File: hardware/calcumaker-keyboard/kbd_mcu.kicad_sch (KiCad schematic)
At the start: 8 parts, among them J2 SWD TC2030-NL, U1 STM32G031K8U6

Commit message: hardware: MCU -> STM32U575RGT6 (LQFP-64) + 4MB QSPI flash; monospace wiring notes
MCU package + external flash
- Swap U1 STM32U575ZGT6 (LQFP-144) -> STM32U575RGT6 (LQFP-64, LCSC C5270980).
  The firmware links at ~323 KB so 1 MB flash is ample (~3x headroom), and with
  the key matrix scanned off-board the LQFP-64 has enough GPIO — smaller/cheaper.
- Correct the flash size everywhere: the STM32 `G` code = 1 MB (not 2 MB; the
  `I` parts are 2 MB). memory.x FLASH 2048K -> 1024K; .cargo runner -> RGTx.
- Add U7 W25Q32JVSSIQ, a 4 MB (32 Mbit) quad-SPI NOR (LCSC C179173, SOIC-8) on
  OCTOSPI1 as a new QSPIFlash sheet (+ R9 CS# pull-up + C26 decoupling) for
  memory-mapped (XIP) constants + state/program storage.
- mcu board 52 -> 55 components / 7 sheets. Docs (DESIGN.md, PARTS.md, READMEs,
  CLAUDE/AGENTS) updated; availability ladder now lists RGT6/VGT6/ZGT6.

Monospace, multi-line schematic wiring notes
- kschgen text_note() now renders notes in a monospace font (Courier New) so
  tables/columns line up; add note_block() + pin_table() helpers.
- Reformat all 14 per-sheet notes into titled, multi-line, aligned blocks —
  connector pinouts as PIN/SIGNAL tables, power/MCU sheets as wiring blocks.

The regenerated schematics carry both changes, so this is one commit. All three
boards regenerate + pass the structure check (mcu 55 / keyboard 119 / display
60, no duplicate refs).

Co-Authored-By: Claude Opus 4.8 (1M context) <noreply@anthropic.com>
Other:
- note added: "SCANNER MCU - U1 STM32G031K8U6 (LCSC C432207, UFQFPN-32) PLACED, not wired. POWER VDD -> +3V3 C1/C2 100nF + C4 4.7uF bulk VDDA -> C3 100nF VSS/EP -> GND RESET / BOOT NRST -> C5 100nF (also -> KB_NRST on J1: U575 can reset it) BOOT0 -> R6 10k to GND (also -> KB_BOOT0 on J1: ROM UART/DFU reflash) CLOCK internal HSI, no crystal. MATRIX 5 ROW (out) + 10 COL (in, int. pull-ups) -> Keypad sheet; hold R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"
- note removed: "Calcumaker 16 keyboard — Scanner MCU U1 STM32G031K8U6 (LCSC C432207, UFQFPN-32). PLACED, not wired. POWER: VDD -> +3V3 (C1/C2 100nF + C4 4.7uF bulk); VDDA -> C3 100nF; VSS/EP -> GND. RESET: NRST + C5 100nF (also -> KB_NRST on J1 so the MCU can reset it). BOOT0 -> R6 10k to GND (also -> KB_BOOT0 on J1 for ROM UART/DFU reflash). CLOCK: internal HSI, no crystal. MATRIX: 5 ROW (out) + 10 COL (in, int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"
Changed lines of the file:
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@@
 		(instances
 			(project "calcumaker-keyboard"
-				(path "/ca1c0000-0000-4000-8000-00000000eb01/6aa00c6d-c4c7-4ac8-98e2-2764bb39a4cb"
+				(path "/ca1c0000-0000-4000-8000-00000000eb01/4dd7cdeb-aa77-4ab0-b654-f9a7d07f70a8"
 					(reference "U1")
 					(unit 1)
@@
 		(instances
 			(project "calcumaker-keyboard"
-				(path "/ca1c0000-0000-4000-8000-00000000eb01/6aa00c6d-c4c7-4ac8-98e2-2764bb39a4cb"
+				(path "/ca1c0000-0000-4000-8000-00000000eb01/4dd7cdeb-aa77-4ab0-b654-f9a7d07f70a8"
 					(reference "C1")
 					(unit 1)
@@
 		(instances
 			(project "calcumaker-keyboard"
-				(path "/ca1c0000-0000-4000-8000-00000000eb01/6aa00c6d-c4c7-4ac8-98e2-2764bb39a4cb"
+				(path "/ca1c0000-0000-4000-8000-00000000eb01/4dd7cdeb-aa77-4ab0-b654-f9a7d07f70a8"
 					(reference "C2")
 					(unit 1)
@@
 		(instances
 			(project "calcumaker-keyboard"
-				(path "/ca1c0000-0000-4000-8000-00000000eb01/6aa00c6d-c4c7-4ac8-98e2-2764bb39a4cb"
+				(path "/ca1c0000-0000-4000-8000-00000000eb01/4dd7cdeb-aa77-4ab0-b654-f9a7d07f70a8"
 					(reference "C3")
 					(unit 1)
@@
 		(instances
 			(project "calcumaker-keyboard"
-				(path "/ca1c0000-0000-4000-8000-00000000eb01/6aa00c6d-c4c7-4ac8-98e2-2764bb39a4cb"
+				(path "/ca1c0000-0000-4000-8000-00000000eb01/4dd7cdeb-aa77-4ab0-b654-f9a7d07f70a8"
 					(reference "C4")
 					(unit 1)
@@
 		(instances
 			(project "calcumaker-keyboard"
-				(path "/ca1c0000-0000-4000-8000-00000000eb01/6aa00c6d-c4c7-4ac8-98e2-2764bb39a4cb"
+				(path "/ca1c0000-0000-4000-8000-00000000eb01/4dd7cdeb-aa77-4ab0-b654-f9a7d07f70a8"
 					(reference "C5")
 					(unit 1)
@@
 		(instances
 			(project "calcumaker-keyboard"
-				(path "/ca1c0000-0000-4000-8000-00000000eb01/6aa00c6d-c4c7-4ac8-98e2-2764bb39a4cb"
+				(path "/ca1c0000-0000-4000-8000-00000000eb01/4dd7cdeb-aa77-4ab0-b654-f9a7d07f70a8"
 					(reference "R6")
 					(unit 1)
@@
 		(instances
 			(project "calcumaker-keyboard"
-				(path "/ca1c0000-0000-4000-8000-00000000eb01/6aa00c6d-c4c7-4ac8-98e2-2764bb39a4cb"
+				(path "/ca1c0000-0000-4000-8000-00000000eb01/4dd7cdeb-aa77-4ab0-b654-f9a7d07f70a8"
 					(reference "J2")
 					(unit 1)
@@
 		)
 	)
-	(text "Calcumaker 16 keyboard — Scanner MCU U1 STM32G031K8U6 (LCSC C432207, UFQFPN-32). PLACED, not wired. POWER: VDD -> +3V3 (C1/C2 100nF + C4 4.7uF bulk); VDDA -> C3 100nF; VSS/EP -> GND. RESET: NRST + C5 100nF (also -> KB_NRST on J1 so the MCU can reset it). BOOT0 -> R6 10k to GND (also -> KB_BOOT0 on J1 for ROM UART/DFU reflash). CLOCK: internal HSI, no crystal. MATRIX: 5 ROW (out) + 10 COL (in, internal pull-ups) -> Keypad sheet; hold ROWs low + COL EXTI for wake-from-Stop. ANNUNCIATORS: 5 GPIO -> the LED resistors (Annunciators sheet). LINK to the U575 (via J1 mezzanine): I2C1 SDA/SCL (reports keys, receives annunciator state) + USART TX/RX (alt/expansion + bootloader) + KB_IRQ out (wakes the U575). PROGRAMMING: J2 SWD Tag-Connect (bare pads) or the UART/DFU bootloader over J1. See DESIGN.md Low-power & wake."
+	(text "SCANNER MCU  -  U1  STM32G031K8U6  (LCSC C432207, UFQFPN-32)\nPLACED, not wired.\n\nPOWER\n  VDD  -> +3V3   C1/C2 100nF + C4 4.7uF bulk\n  VDDA -> C3 100nF          VSS/EP -> GND\nRESET / BOOT\n  NRST  -> C5 100nF  (also -> KB_NRST on J1: U575 can reset it)\n  BOOT0 -> R6 10k to GND (also -> KB_BOOT0 on J1: ROM UART/DFU reflash)\nCLOCK   internal HSI, no crystal.\n\nMATRIX  5 ROW (out) + 10 COL (in, int. pull-ups) -> Keypad sheet;\n        hold ROWs low + COL EXTI for wake-from-Stop.\nANNUN   5 GPIO -> the LED resistors (Annunciators sheet).\nLINK (via J1 mezzanine to the U575)\n  I2C1  SDA/SCL  reports keys, receives annunciator state\n  USART TX/RX    alt/expansion + bootloader\n  KB_IRQ (out)   wakes the U575\nPROG    J2 SWD Tag-Connect (bare pads) or UART/DFU over J1.\nSee DESIGN.md Low-power & wake."
 		(exclude_from_sim no)
 		(at 15.00 150.00 0)
-		(effects (font (size 1.5 1.5)) (justify left top))
+		(effects (font (face "Courier New") (size 1.27 1.27)) (justify left top))
 	)
 	(sheet_instances

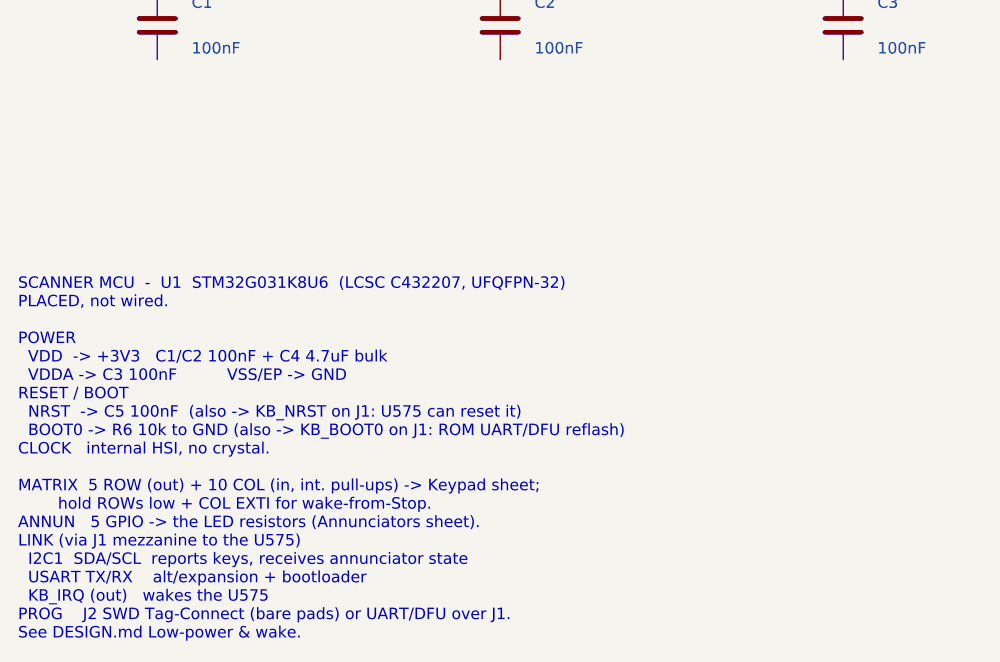
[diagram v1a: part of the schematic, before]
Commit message: hardware: per-key RGB hint lighting on the keyboard board (50x SK6805 on gated VSYS) (#4)
Add addressable RGB accent lighting that hints key positions / presses -- one
SK6805-EC15 (1.5x1.5mm, the smallest serial RGB with a KiCad footprint + real
LCSC stock, C2890035) beside each of the 50 keys, single-wire daisy chain off
one STM32G0 pin.

Power: the LEDs are ~5V parts and the keyboard rail is only 3.3V, so they run
off VSYS (the MCU board's load-shared battery/USB rail, ~3.7-4.7V) brought up a
WIDENED 12-pin mezzanine (10 -> 12: +VSYS +GND). A high-side P-FET load switch
(Q1 AO3401A + Q2 2N7002) gates the whole LED rail off in sleep (G0 LED_EN) to
protect battery life, and a 74LVC1G125 (powered from the gated rail) level-shifts
the 3.3V data up to the LED VIH.

- calcumaker-keyboard: new KeyLighting sheet (50x SK6805 D56-D105 + U2 shifter +
  Q1/Q2 load switch + R7-R10 / C6-C7); J1 mezzanine -> 12-pin DF40C-12DP
  (C6224952). 119 -> 178 components.
- calcumaker-mcu: J5 mezzanine -> 12-pin DF40B-12DS (C3641147); route VSYS.
- DF40 stack: the receptacle SUFFIX sets the mated height (none = 1.5mm,
  (2.0) = 2.0mm, H-series = 2.5-4.0mm), NOT the B/C letter; the DF40C plug is the
  common header -- so DF40C-12DP x DF40B-12DS is a valid 1.5mm stack, same as the
  original 10-pin (DF40C-12DS just isn't LCSC-stocked).
- DESIGN.md / PARTS.md / memory: RGB subsystem, 12-pin pinout, BOM rows, the
  sleep-gate + current-cap notes (firmware must cap total brightness; 50x
  full-white ~0.75A would exceed the DF40 / VSYS budget).

All three boards regenerate + pass the structure check (mcu 55 / keyboard 178 /
display 60, no duplicate refs).

Co-authored-by: Claude Opus 4.8 (1M context) <noreply@anthropic.com>
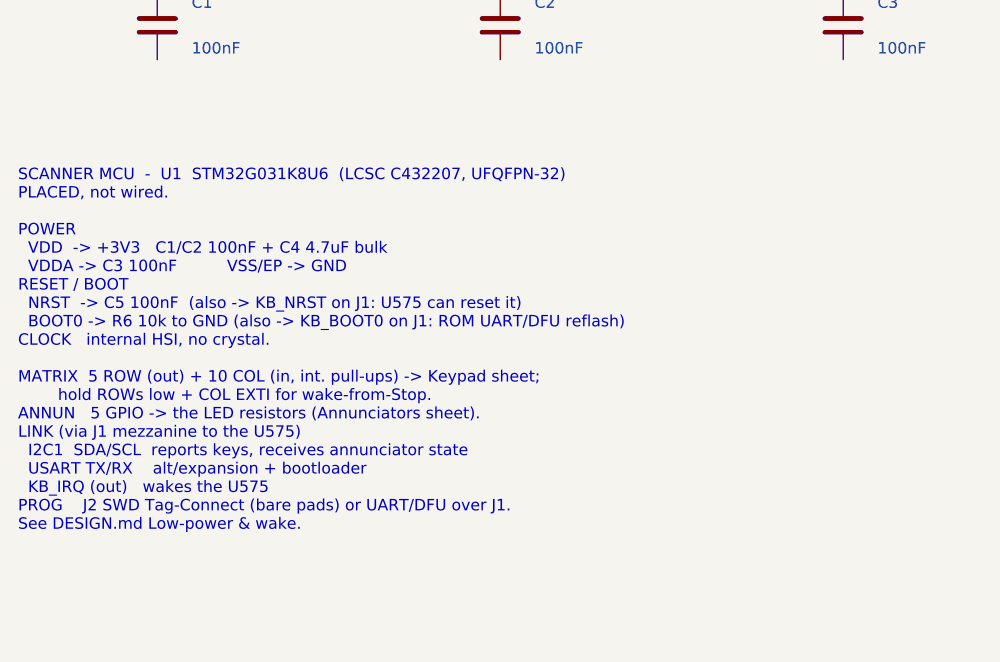
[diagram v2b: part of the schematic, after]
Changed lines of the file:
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@@
 	(title_block
 		(title "Calcumaker 16 — Keyboard — Keyboard scanner MCU (STM32G031K8U6)")
-		(date "2026-07-05")
-		(rev "0.2")
+		(date "2026-07-06")
+		(rev "0.3")
 		(company "calcumaker authors")
 	)
@@
 	(text "SCANNER MCU  -  U1  STM32G031K8U6  (LCSC C432207, UFQFPN-32)\nPLACED, not wired.\n\nPOWER\n  VDD  -> +3V3   C1/C2 100nF + C4 4.7uF bulk\n  VDDA -> C3 100nF          VSS/EP -> GND\nRESET / BOOT\n  NRST  -> C5 100nF  (also -> KB_NRST on J1: U575 can reset it)\n  BOOT0 -> R6 10k to GND (also -> KB_BOOT0 on J1: ROM UART/DFU reflash)\nCLOCK   internal HSI, no crystal.\n\nMATRIX  5 ROW (out) + 10 COL (in, int. pull-ups) -> Keypad sheet;\n        hold ROWs low + COL EXTI for wake-from-Stop.\nANNUN   5 GPIO -> the LED resistors (Annunciators sheet).\nLINK (via J1 mezzanine to the U575)\n  I2C1  SDA/SCL  reports keys, receives annunciator state\n  USART TX/RX    alt/expansion + bootloader\n  KB_IRQ (out)   wakes the U575\nPROG    J2 SWD Tag-Connect (bare pads) or UART/DFU over J1.\nSee DESIGN.md Low-power & wake."
 		(exclude_from_sim no)
-		(at 15.00 150.00 0)
+		(at 15.00 137.92 0)
 		(effects (font (face "Courier New") (size 1.27 1.27)) (justify left top))
 	)

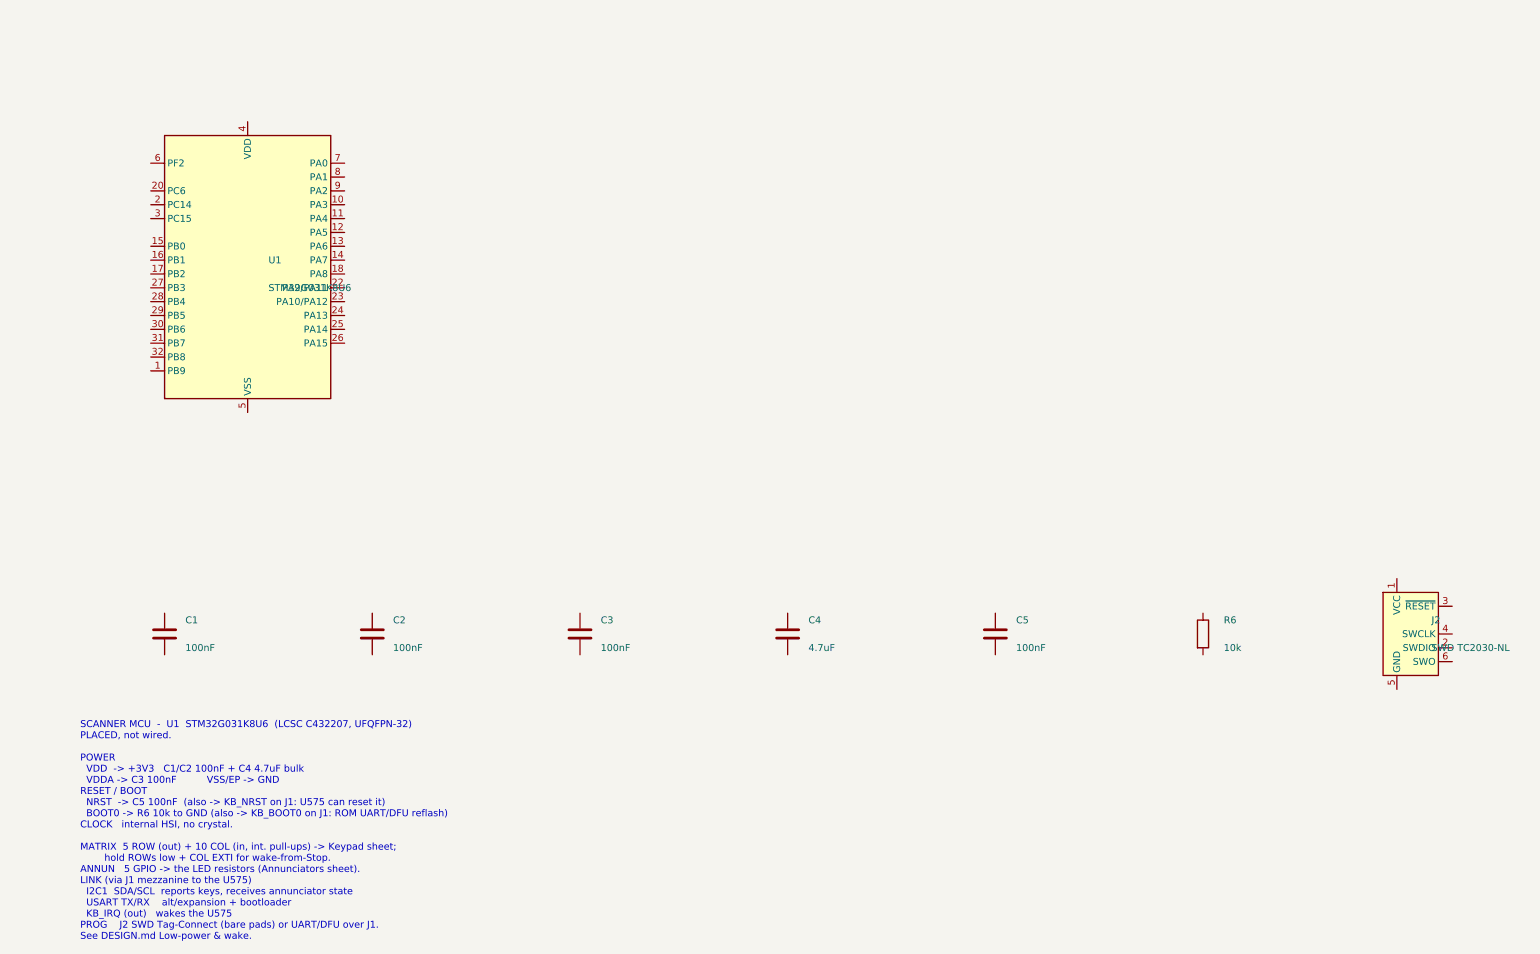
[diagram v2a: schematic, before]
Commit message: hardware: keyboard as a multi-channel design (reusable 10-key row x5) (#5)
Refactor calcumaker-keyboard from a FLAT layout (100 individually-placed SW/D
parts on one sheet + 50 flat RGB LEDs) into a KiCad multi-channel design,
matching the display board.

- key_row.kicad_sch: a reusable 10-key row, FULLY WIRED, instantiated x5
  (Row1-5). Each key = MX switch + 1N4148W diode + SK6805 RGB.
    matrix  SW.1 -> ROW (hier); SW.2 -> KNk -> diode.A; diode.K -> COLk (global)
    RGB     DIN -> LED1..LED10 -> DOUT (hier, chained @root); VDD->VLED, VSS->GND
  Per-instance refs SW1-50 / D1-50 (matrix) / D56-105 (RGB). Shared buses
  (COL1-10, VLED, GND) are global nets; ROW + RGB DIN/DOUT are hierarchical pins
  wired at the root (KB_ROW1-5; KB_LED_DATA -> Row1 -> ... -> Row5 -> RGB_END).
- Split the old KeyLighting sheet -> key_row (the 50 LEDs) + rgb_power (the
  level shifter + gated load switch).
- Converted the whole keyboard manifest from the flat K.build() path to the
  display-style write_wired_child/write_root API; the one-off sheets
  (annunc/kbd_mcu/rgb_power/main_if) stay single-instance, placed via a grid
  helper. Removed the obsolete keypad.kicad_sch + keylight.kicad_sch.
- Docs (DESIGN.md sheet plan, CLAUDE/AGENTS, scripts README) + a few stale fixes
  (STM32U575RGTx, "three boards", current sheet names).

178 components, no duplicate refs, all three boards pass the structure check.
(The 2 lib_symbol_mismatch ERC warnings on the G0/TagConnect are pre-existing
kschgen symbol-cache fidelity, not from this change.)

Co-authored-by: Claude Opus 4.8 (1M context) <noreply@anthropic.com>
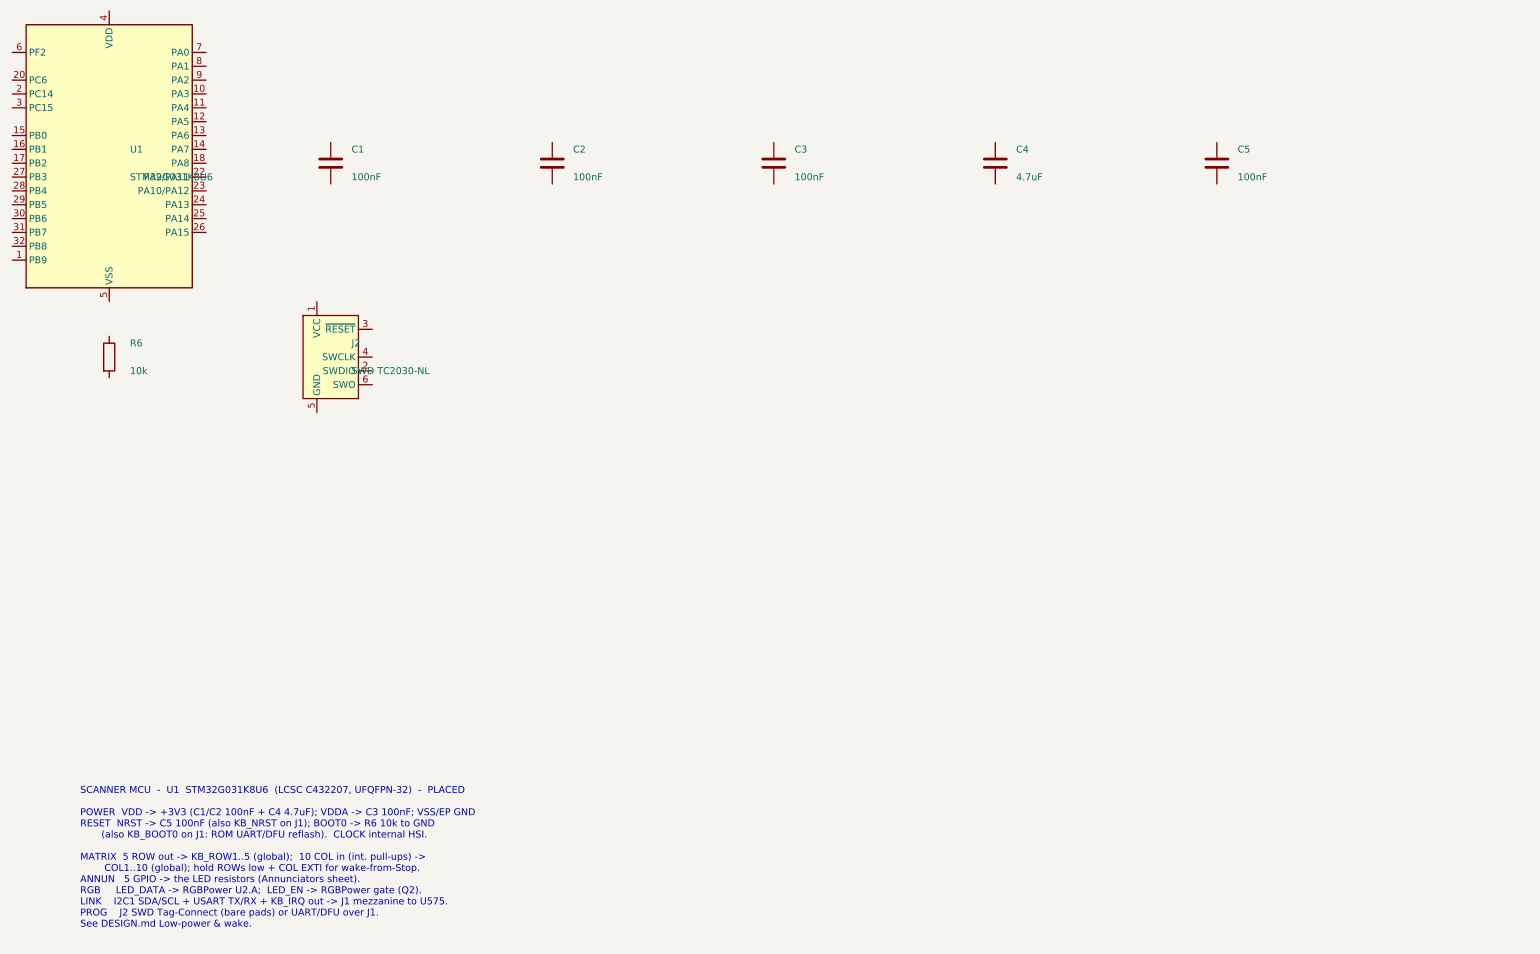
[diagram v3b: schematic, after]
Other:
- note added: "SCANNER MCU - U1 STM32G031K8U6 (LCSC C432207, UFQFPN-32) - PLACED POWER VDD -> +3V3 (C1/C2 100nF + C4 4.7uF); VDDA -> C3 100nF; VSS/EP GND RESET NRST -> C5 100nF (also KB_NRST on J1); BOOT0 -> R6 10k to GND (also KB_BOOT0 on J1: ROM UART/DFU reflash). CLOCK internal HSI. MATRIX 5 ROW out -> KB_ROW1..5 (global); 10 COL in (int. pull-ups) -> COL1..10 (global); hold ROWs low + COL EXTI for wake-from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"
- note removed: "SCANNER MCU - U1 STM32G031K8U6 (LCSC C432207, UFQFPN-32) PLACED, not wired. POWER VDD -> +3V3 C1/C2 100nF + C4 4.7uF bulk VDDA -> C3 100nF VSS/EP -> GND RESET / BOOT NRST -> C5 100nF (also -> KB_NRST on J1: U575 can reset it) BOOT0 -> R6 10k to GND (also -> KB_BOOT0 on J1: ROM UART/DFU reflash) CLOCK internal HSI, no crystal. MATRIX 5 ROW (out) + 10 COL (in, int. pull-ups) -> Keypad sheet; hold R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"
